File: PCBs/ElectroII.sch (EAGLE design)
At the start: 35 parts, among them J1 U.FL-R-SMT(01), T1 VIN, T2 VBAT, T3 GND, T4 5V, T5 VCC, U1 RFM95W-868S2, U2 TPS61090RSAR

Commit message: Fixed MOSI/MISO mistake
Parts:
- added T6: ANT, RTR Main Library:TEST_PAD
- C2: value 100u -> 47u
- R1: value 1.85M -> 1.8M
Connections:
- net ANT: now also T6.P$1
- net MISO: now also U1.MISO; no longer U1.MOSI
- net MOSI: now also U1.MOSI; no longer U1.MISO
- net UART0_GPIO0: now also UART0.4; no longer UART0.6
- net UART0_GPIO1: now also UART0.6; no longer UART0.8
- net UART0_GPIO2: now also UART0.8; no longer UART0.10
- net UART0_GPIO3: now also UART0.10; no longer UART0.12
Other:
- moved on the sheet: J1
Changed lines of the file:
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@@
 <part name="GND17" library="RTR Main Library" deviceset="GND" device=""/>
 <part name="GND18" library="RTR Main Library" deviceset="GND" device=""/>
-<part name="C2" library="RTR Main Library" deviceset="C-ALL_PACKAGES" device="C1206" value="100u"/>
+<part name="C2" library="RTR Main Library" deviceset="C-ALL_PACKAGES" device="C1206" value="47u"/>
 <part name="GND19" library="RTR Main Library" deviceset="GND" device=""/>
 <part name="GND20" library="RTR Main Library" deviceset="GND" device=""/>
 <part name="GND21" library="RTR Main Library" deviceset="GND" device=""/>
 <part name="L1" library="RTR Main Library" deviceset="L_SMD" device="" value="6.8u"/>
-<part name="R1" library="RTR Main Library" deviceset="R-ALL_PACKAGES" device="R1206" value="1.85M"/>
+<part name="R1" library="RTR Main Library" deviceset="R-ALL_PACKAGES" device="R1206" value="1.8M"/>
 <part name="R2" library="RTR Main Library" deviceset="R-ALL_PACKAGES" device="R1206" value="200k"/>
 <part name="R3" library="RTR Main Library" deviceset="R-ALL_PACKAGES" device="R1206" value="1.1M"/>
@@
 <part name="T4" library="RTR Main Library" deviceset="TEST_PAD" device="" value="5V"/>
 <part name="T5" library="RTR Main Library" deviceset="TEST_PAD" device="" value="VCC"/>
+<part name="T6" library="RTR Main Library" deviceset="TEST_PAD" device="" value="ANT"/>
 </parts>
 <sheets>
@@
 <wire x1="-279.4" y1="-68.58" x2="-279.4" y2="-7.62" width="0.1524" layer="97"/>
 <text x="-175.26" y="-12.7" size="1.778" layer="97">BOOST CONVERTER</text>
-<text x="-259.08" y="-17.78" size="1.778" layer="97">PTC FUSE</text>
+<text x="-256.54" y="-17.78" size="1.778" layer="97">PTC FUSE</text>
 </plain>
 <instances>
@@
 <attribute name="VALUE" x="-48.26" y="-22.86" size="1.778" layer="96"/>
 </instance>
-<instance part="J1" gate="G$1" x="48.26" y="-104.14" smashed="yes">
-<attribute name="NAME" x="44.44143125" y="-100.06686875" size="1.27285" layer="95"/>
-<attribute name="VALUE" x="43.93218125" y="-109.7407" size="1.27288125" layer="96"/>
-</instance>
-<instance part="GND15" gate="1" x="38.1" y="-109.22" smashed="yes">
-<attribute name="VALUE" x="35.56" y="-111.76" size="1.778" layer="96"/>
+<instance part="J1" gate="G$1" x="55.88" y="-104.14" smashed="yes">
+<attribute name="NAME" x="52.06143125" y="-100.06686875" size="1.27285" layer="95"/>
+<attribute name="VALUE" x="51.55218125" y="-109.7407" size="1.27288125" layer="96"/>
+</instance>
+<instance part="GND15" gate="1" x="45.72" y="-109.22" smashed="yes">
+<attribute name="VALUE" x="43.18" y="-111.76" size="1.778" layer="96"/>
 </instance>
 <instance part="C1" gate="G$1" x="35.56" y="-88.9" smashed="yes">
@@
 </instance>
 <instance part="D1" gate="1" x="-233.68" y="-25.4" smashed="yes" rot="R90">
-<attribute name="NAME" x="-234.1626" y="-22.86" size="1.778" layer="95" rot="R90"/>
-<attribute name="VALUE" x="-231.3686" y="-22.86" size="1.778" layer="96" rot="R90"/>
+<attribute name="NAME" x="-231.14" y="-15.7226" size="1.778" layer="95" rot="R180"/>
+<attribute name="VALUE" x="-228.6" y="-18.0086" size="1.778" layer="96" rot="R180"/>
 </instance>
 <instance part="GND24" gate="1" x="-233.68" y="-30.48" smashed="yes">
@@
 <attribute name="NAME" x="-33.02" y="40.64" size="1.778" layer="95"/>
 <attribute name="VALUE" x="-33.02" y="38.1" size="1.778" layer="96"/>
+</instance>
+<instance part="T6" gate="G$1" x="45.72" y="-99.06" smashed="yes">
+<attribute name="NAME" x="40.64" y="-91.44" size="1.778" layer="95"/>
+<attribute name="VALUE" x="40.64" y="-93.98" size="1.778" layer="96"/>
 </instance>
 </instances>
@@
 </segment>
 <segment>
-<pinref part="UART0" gate="G$1" pin="6"/>
-<wire x1="104.14" y1="-58.42" x2="106.68" y2="-58.42" width="0.1524" layer="91"/>
-<label x="106.68" y="-58.42" size="1.778" layer="95"/>
+<pinref part="UART0" gate="G$1" pin="4"/>
+<wire x1="104.14" y1="-55.88" x2="106.68" y2="-55.88" width="0.1524" layer="91"/>
+<label x="106.68" y="-55.88" size="1.778" layer="95"/>
 </segment>
 </net>
@@
 </segment>
 <segment>
-<pinref part="U1" gate="G$1" pin="MISO"/>
-<wire x1="-15.24" y1="-96.52" x2="-33.02" y2="-96.52" width="0.1524" layer="91"/>
-<label x="-33.02" y="-96.52" size="1.778" layer="95"/>
+<pinref part="U1" gate="G$1" pin="MOSI"/>
+<wire x1="20.32" y1="-109.22" x2="25.4" y2="-109.22" width="0.1524" layer="91"/>
+<label x="25.4" y="-109.22" size="1.778" layer="95"/>
 </segment>
 </net>
@@
 </segment>
 <segment>
-<pinref part="U1" gate="G$1" pin="MOSI"/>
-<wire x1="20.32" y1="-109.22" x2="25.4" y2="-109.22" width="0.1524" layer="91"/>
-<label x="25.4" y="-109.22" size="1.778" layer="95"/>
+<pinref part="U1" gate="G$1" pin="MISO"/>
+<wire x1="-15.24" y1="-96.52" x2="-33.02" y2="-96.52" width="0.1524" layer="91"/>
+<label x="-33.02" y="-96.52" size="1.778" layer="95"/>
 </segment>
 </net>
@@
 <net name="UART0_GPIO1" class="0">
 <segment>
+<pinref part="U$1" gate="G$1" pin="GPIO27/GEN2"/>
+<wire x1="-22.86" y1="15.24" x2="-40.64" y2="15.24" width="0.1524" layer="91"/>
+<label x="-40.64" y="15.24" size="1.778" layer="95"/>
+</segment>
+<segment>
+<pinref part="UART0" gate="G$1" pin="6"/>
+<wire x1="104.14" y1="-58.42" x2="106.68" y2="-58.42" width="0.1524" layer="91"/>
+<label x="106.68" y="-58.42" size="1.778" layer="95"/>
+</segment>
+</net>
+<net name="UART0_GPIO2" class="0">
+<segment>
+<pinref part="U$1" gate="G$1" pin="GPIO22/GEN3"/>
+<wire x1="-22.86" y1="12.7" x2="-40.64" y2="12.7" width="0.1524" layer="91"/>
+<label x="-40.64" y="12.7" size="1.778" layer="95"/>
+</segment>
+<segment>
 <pinref part="UART0" gate="G$1" pin="8"/>
 <wire x1="104.14" y1="-60.96" x2="106.68" y2="-60.96" width="0.1524" layer="91"/>
 <label x="106.68" y="-60.96" size="1.778" layer="95"/>
 </segment>
-<segment>
-<pinref part="U$1" gate="G$1" pin="GPIO27/GEN2"/>
-<wire x1="-22.86" y1="15.24" x2="-40.64" y2="15.24" width="0.1524" layer="91"/>
-<label x="-40.64" y="15.24" size="1.778" layer="95"/>
-</segment>
-</net>
-<net name="UART0_GPIO2" class="0">
+</net>
+<net name="UART0_GPIO3" class="0">
+<segment>
+<pinref part="U$1" gate="G$1" pin="GPIO5"/>
+<wire x1="-22.86" y1="-5.08" x2="-40.64" y2="-5.08" width="0.1524" layer="91"/>
+<label x="-40.64" y="-5.08" size="1.778" layer="95"/>
+</segment>
 <segment>
 <pinref part="UART0" gate="G$1" pin="10"/>
@@
 <label x="106.68" y="-63.5" size="1.778" layer="95"/>
 </segment>
-<segment>
-<pinref part="U$1" gate="G$1" pin="GPIO22/GEN3"/>
-<wire x1="-22.86" y1="12.7" x2="-40.64" y2="12.7" width="0.1524" layer="91"/>
-<label x="-40.64" y="12.7" size="1.778" layer="95"/>
-</segment>
-</net>
-<net name="UART0_GPIO3" class="0">
-<segment>
-<pinref part="UART0" gate="G$1" pin="12"/>
-<wire x1="104.14" y1="-66.04" x2="106.68" y2="-66.04" width="0.1524" layer="91"/>
-<label x="106.68" y="-66.04" size="1.778" layer="95"/>
-</segment>
-<segment>
-<pinref part="U$1" gate="G$1" pin="GPIO5"/>
-<wire x1="-22.86" y1="-5.08" x2="-40.64" y2="-5.08" width="0.1524" layer="91"/>
-<label x="-40.64" y="-5.08" size="1.778" layer="95"/>
-</segment>
 </net>
 <net name="ANT" class="3">
@@
 <pinref part="U1" gate="G$1" pin="ANT"/>
 <pinref part="J1" gate="G$1" pin="SIG"/>
-<wire x1="20.32" y1="-101.6" x2="38.1" y2="-101.6" width="0.1524" layer="91"/>
+<wire x1="20.32" y1="-101.6" x2="45.72" y2="-101.6" width="0.1524" layer="91"/>
 <label x="22.86" y="-101.6" size="1.778" layer="95"/>
-</segment>
-</net>
+<pinref part="T6" gate="G$1" pin="P$1"/>
+<junction x="45.72" y="-101.6"/>
+</segment>
+</net>

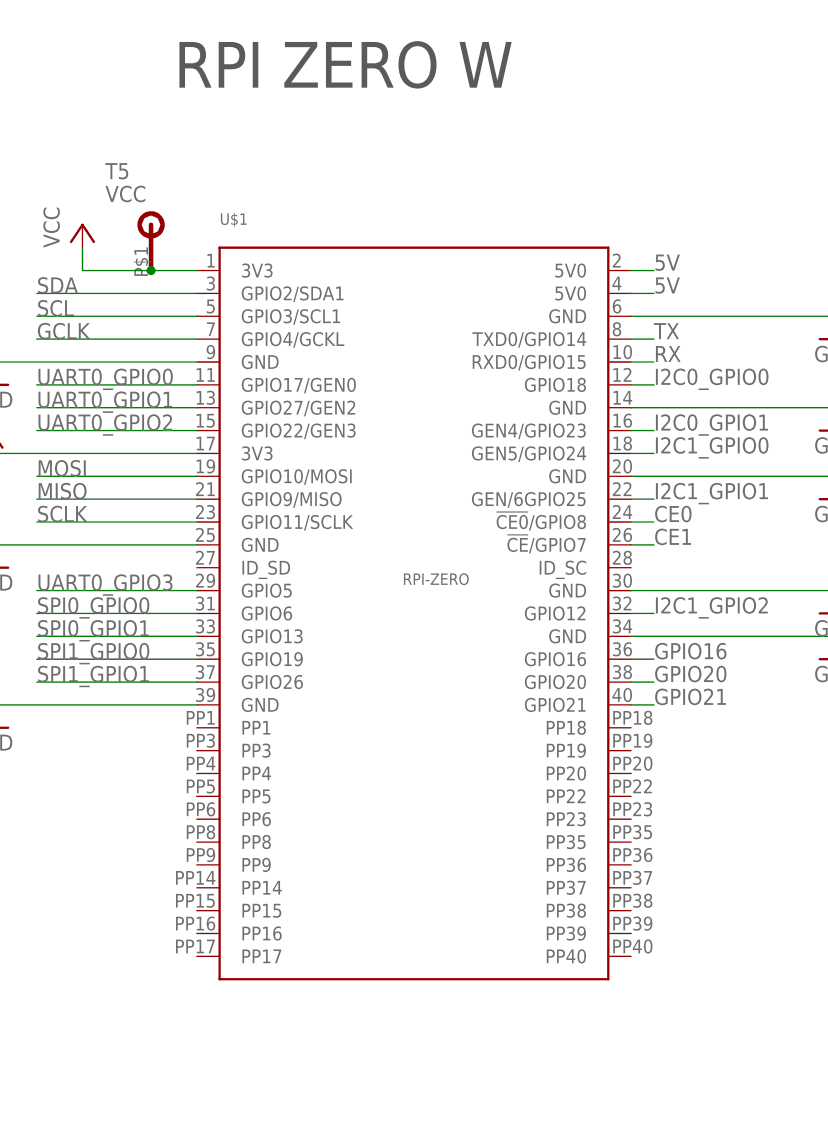
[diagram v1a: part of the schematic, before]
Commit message: Updated RPi library
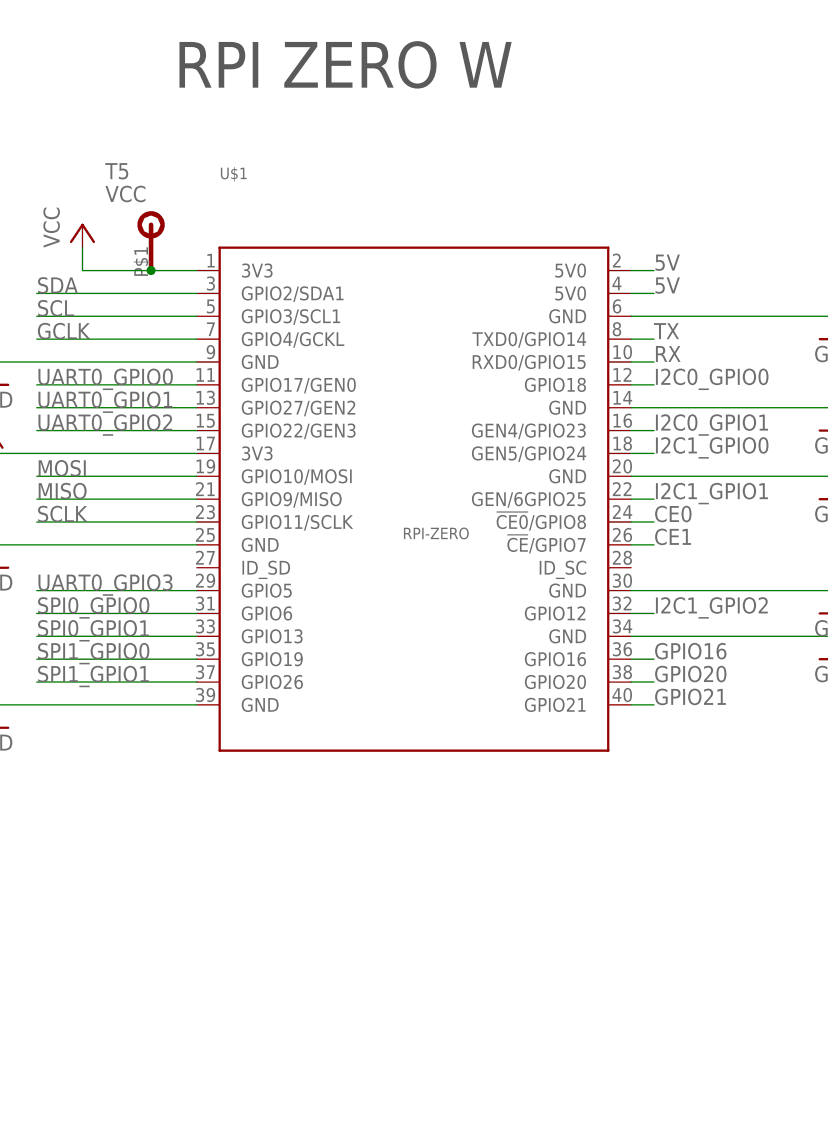
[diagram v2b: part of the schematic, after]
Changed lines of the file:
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@@
 </plain>
 <instances>
-<instance part="U$1" gate="G$1" x="0" y="0" smashed="yes">
-<attribute name="NAME" x="-20.32" y="35.56" size="1.27" layer="95" font="vector"/>
-<attribute name="VALUE" x="0" y="-4.445" size="1.27" layer="96" font="vector"/>
+<instance part="U$1" gate="G$1" x="0" y="5.08" smashed="yes">
+<attribute name="NAME" x="-20.32" y="40.64" size="1.27" layer="95" font="vector"/>
+<attribute name="VALUE" x="0" y="0.635" size="1.27" layer="96" font="vector"/>
 </instance>
 <instance part="SPI0" gate="G$1" x="96.52" y="33.02" smashed="yes">

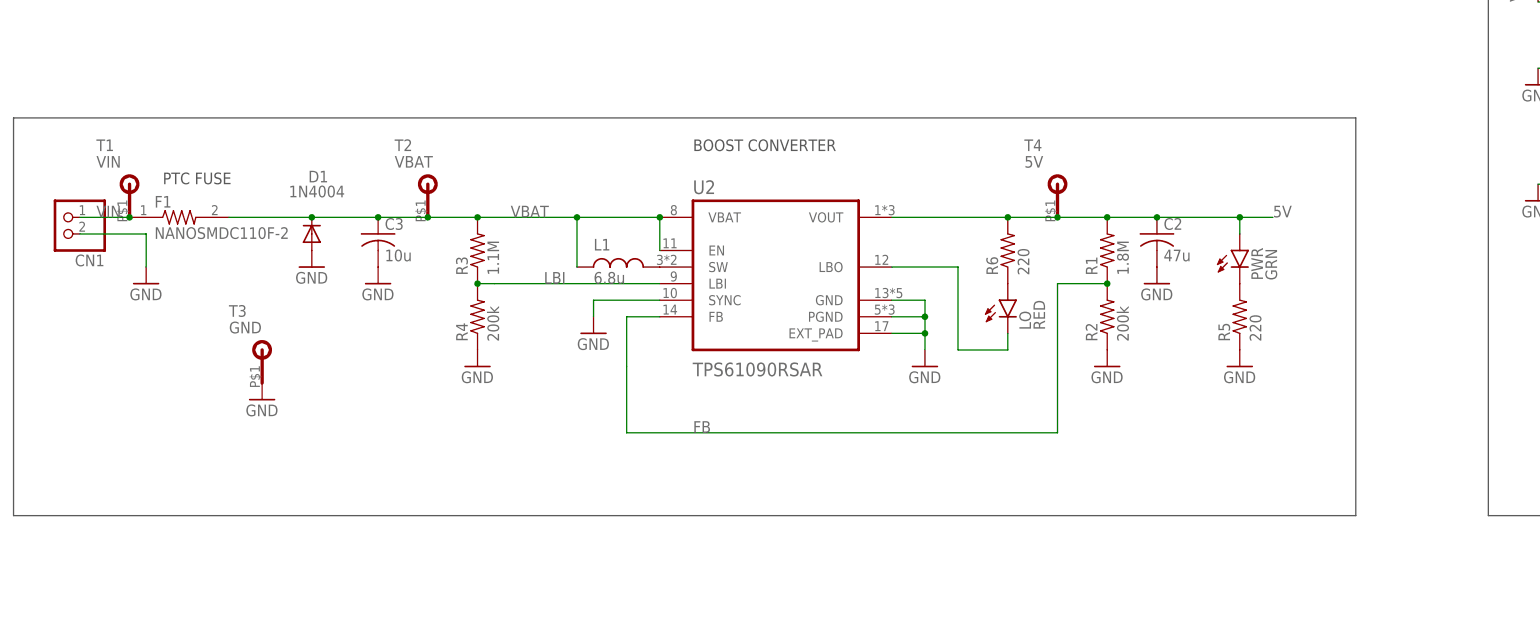
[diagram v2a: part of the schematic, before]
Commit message: Board shake-ups from design review
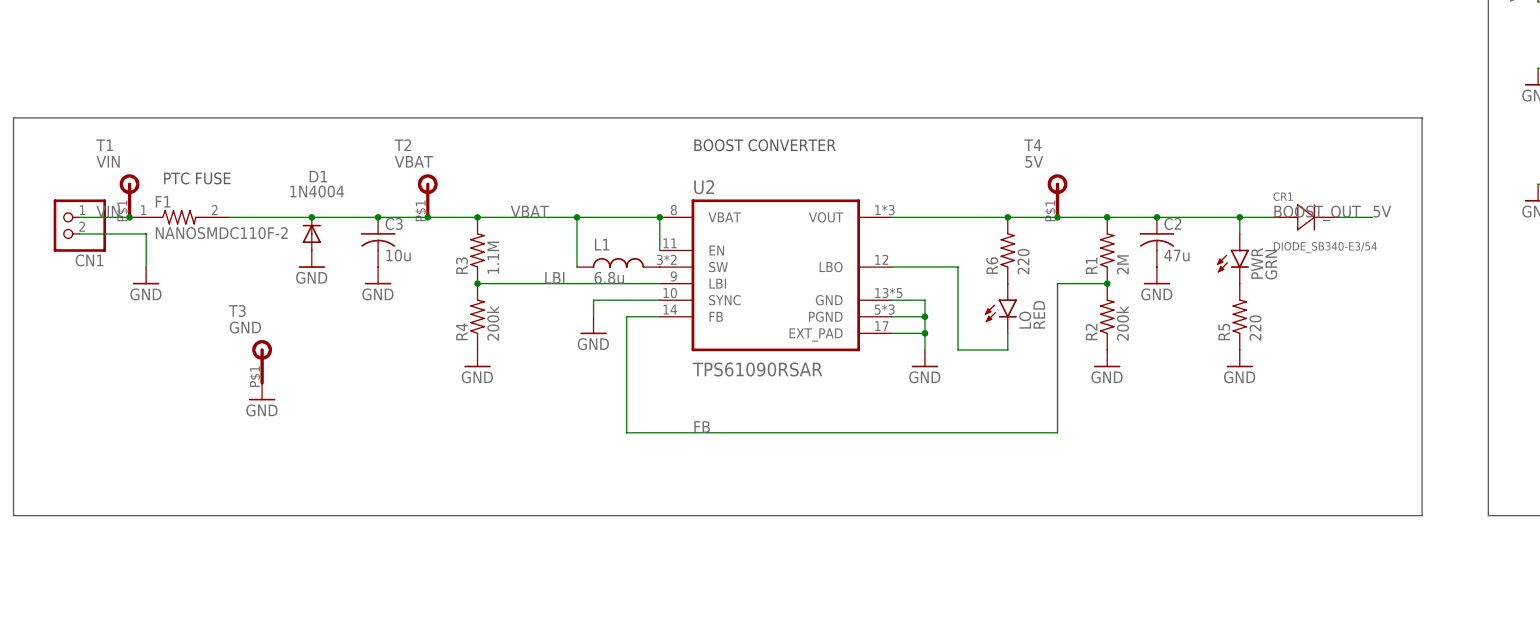
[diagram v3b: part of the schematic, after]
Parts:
- added CR1: DIODE_SB340-E3/54, DIODE_SB340-E3-54:DIODE_SB340-E3/54
- R1: value 1.8M -> 2M
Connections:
- new net BOOST_OUT: C2.1, CR1.2, PWR.A, R1.2, R6.2, T4.P$1, U2.VOUT
- net 5V: now also CR1.1; no longer C2.1, PWR.A, R1.2, R6.2, T4.P$1, U2.VOUT
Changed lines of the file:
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@@
 <part name="GND21" library="RTR Main Library" deviceset="GND" device=""/>
 <part name="L1" library="RTR Main Library" deviceset="L_SMD" device="" value="6.8u"/>
-<part name="R1" library="RTR Main Library" deviceset="R-ALL_PACKAGES" device="R1206" value="1.8M"/>
+<part name="R1" library="RTR Main Library" deviceset="R-ALL_PACKAGES" device="R1206" value="2M"/>
 <part name="R2" library="RTR Main Library" deviceset="R-ALL_PACKAGES" device="R1206" value="200k"/>
 <part name="R3" library="RTR Main Library" deviceset="R-ALL_PACKAGES" device="R1206" value="1.1M"/>
@@
 <part name="T5" library="RTR Main Library" deviceset="TEST_PAD" device="" value="VCC"/>
 <part name="T6" library="RTR Main Library" deviceset="TEST_PAD" device="" value="ANT"/>
+<part name="CR1" library="DIODE_SB340-E3-54" deviceset="DIODE_SB340-E3/54" device=""/>
 </parts>
 <sheets>
@@
 <wire x1="60.96" y1="-73.66" x2="-43.18" y2="-73.66" width="0.1524" layer="97"/>
 <text x="-25.4" y="-83.82" size="2.54" layer="97">TRANCEIVER</text>
-<wire x1="-279.4" y1="-7.62" x2="-73.66" y2="-7.62" width="0.1524" layer="97"/>
-<wire x1="-73.66" y1="-7.62" x2="-73.66" y2="-68.58" width="0.1524" layer="97"/>
-<wire x1="-73.66" y1="-68.58" x2="-279.4" y2="-68.58" width="0.1524" layer="97"/>
+<wire x1="-279.4" y1="-7.62" x2="-63.5" y2="-7.62" width="0.1524" layer="97"/>
+<wire x1="-63.5" y1="-7.62" x2="-63.5" y2="-68.58" width="0.1524" layer="97"/>
+<wire x1="-63.5" y1="-68.58" x2="-279.4" y2="-68.58" width="0.1524" layer="97"/>
 <wire x1="-279.4" y1="-68.58" x2="-279.4" y2="-7.62" width="0.1524" layer="97"/>
 <text x="-175.26" y="-12.7" size="1.778" layer="97">BOOST CONVERTER</text>
@@
 <attribute name="VALUE" x="40.64" y="-93.98" size="1.778" layer="96"/>
 </instance>
+<instance part="CR1" gate="A" x="-86.36" y="-22.86" smashed="yes">
+<attribute name="VALUE" x="-86.36" y="-27.94" size="1.27" layer="96" ratio="10" rot="SR0"/>
+<attribute name="NAME" x="-86.36" y="-20.32" size="1.27" layer="95" ratio="10" rot="SR0"/>
+</instance>
 </instances>
 <busses>
@@
 </segment>
 <segment>
-<pinref part="U2" gate="G$1" pin="VOUT"/>
-<wire x1="-144.78" y1="-22.86" x2="-127" y2="-22.86" width="0.1524" layer="91"/>
-<wire x1="-127" y1="-22.86" x2="-119.38" y2="-22.86" width="0.1524" layer="91"/>
-<wire x1="-119.38" y1="-22.86" x2="-111.76" y2="-22.86" width="0.1524" layer="91"/>
-<wire x1="-111.76" y1="-22.86" x2="-104.14" y2="-22.86" width="0.1524" layer="91"/>
-<junction x="-111.76" y="-22.86"/>
-<pinref part="C2" gate="G$1" pin="1"/>
-<wire x1="-104.14" y1="-22.86" x2="-91.44" y2="-22.86" width="0.1524" layer="91"/>
-<junction x="-104.14" y="-22.86"/>
-<pinref part="R1" gate="G$1" pin="2"/>
-<junction x="-91.44" y="-22.86"/>
-<wire x1="-91.44" y1="-22.86" x2="-86.36" y2="-22.86" width="0.1524" layer="91"/>
-<pinref part="PWR" gate="G$1" pin="A"/>
-<wire x1="-91.44" y1="-22.86" x2="-91.44" y2="-25.4" width="0.1524" layer="91"/>
-<pinref part="R6" gate="G$1" pin="2"/>
-<junction x="-127" y="-22.86"/>
-<label x="-86.36" y="-22.86" size="1.778" layer="95"/>
-<junction x="-119.38" y="-22.86"/>
-<pinref part="T4" gate="G$1" pin="P$1"/>
+<pinref part="CR1" gate="A" pin="1"/>
+<wire x1="-76.2" y1="-22.86" x2="-71.12" y2="-22.86" width="0.1524" layer="91"/>
+<label x="-71.12" y="-22.86" size="1.778" layer="95"/>
 </segment>
 </net>
@@
 </segment>
 </net>
+<net name="BOOST_OUT" class="1">
+<segment>
+<pinref part="U2" gate="G$1" pin="VOUT"/>
+<wire x1="-144.78" y1="-22.86" x2="-127" y2="-22.86" width="0.1524" layer="91"/>
+<wire x1="-127" y1="-22.86" x2="-119.38" y2="-22.86" width="0.1524" layer="91"/>
+<wire x1="-119.38" y1="-22.86" x2="-111.76" y2="-22.86" width="0.1524" layer="91"/>
+<wire x1="-111.76" y1="-22.86" x2="-104.14" y2="-22.86" width="0.1524" layer="91"/>
+<junction x="-111.76" y="-22.86"/>
+<pinref part="C2" gate="G$1" pin="1"/>
+<wire x1="-104.14" y1="-22.86" x2="-91.44" y2="-22.86" width="0.1524" layer="91"/>
+<junction x="-104.14" y="-22.86"/>
+<pinref part="R1" gate="G$1" pin="2"/>
+<junction x="-91.44" y="-22.86"/>
+<wire x1="-91.44" y1="-22.86" x2="-86.36" y2="-22.86" width="0.1524" layer="91"/>
+<pinref part="PWR" gate="G$1" pin="A"/>
+<wire x1="-91.44" y1="-22.86" x2="-91.44" y2="-25.4" width="0.1524" layer="91"/>
+<pinref part="R6" gate="G$1" pin="2"/>
+<junction x="-127" y="-22.86"/>
+<label x="-86.36" y="-22.86" size="1.778" layer="95"/>
+<junction x="-119.38" y="-22.86"/>
+<pinref part="T4" gate="G$1" pin="P$1"/>
+<pinref part="CR1" gate="A" pin="2"/>
+</segment>
+</net>

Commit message: More board shuffling
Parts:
- added R7, R8: DNP, RTR Main Library:R-ALL_PACKAGESR1206
- added R9: 0.1 1/8w, RTR Main Library:R-ALL_PACKAGESR1206
- T4: value 5V -> BOOST
- T6: value ANT -> 5V
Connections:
- removed net I2C0_GPIO1: I2C0.6, U$1.GEN4/GPIO23
- new net CGND: R9.1
- new net SPI2_GPIO0: U$1.GEN5/GPIO24, U1.RESET
- new net SPI2_GPIO1: U$1.GEN4/GPIO23, U1.DIO0
- net 5V: now also T6.P$1
- net ANT: no longer T6.P$1
- net GND: now also R9.2
- net I2C0_GPIO0: no longer I2C0.4
- net I2C1_GPIO0: no longer U$1.GEN5/GPIO24
- net SCL: now also R8.1
- net SDA: now also R7.1
- net SPI0_GPIO0: no longer U1.RESET
- net SPI0_GPIO1: no longer U1.DIO0
- net VCC: now also R7.2, R8.2
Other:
- moved on the sheet: BRK0, C1, C2, C3, CN1, CR1, D1, F1, I2C0, I2C0_BRK, I2C1, I2C1_BRK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

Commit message: more board shuffling
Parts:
- removed CR1: DIODE_SB340-E3/54, DIODE_SB340-E3-54:DIODE_SB340-E3/54
- added D2: 1N4004, adafruit:1N4004
- R1: value 2M -> 1.96M
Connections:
- net 5V: now also D2.C; no longer CR1.1
- net BOOST_OUT: now also D2.A; no longer CR1.2
- net VBAT: now also CN1.2, F1.1, T1.P$1; no longer C3.1, D1.C, F1.2, L1.1, R3.2, T2.P$1, U2.EN, U2.VBAT
- net VIN: now also C3.1, D1.C, F1.2, L1.1, R3.2, T2.P$1, U2.EN, U2.VBAT; no longer CN1.2, F1.1, T1.P$1
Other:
- note added: "-0.49 V"
- note added: "5.4 V"
- note added: "USE SB340 DIODE"
